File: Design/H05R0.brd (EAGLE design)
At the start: 60 x 34.6 mm, 59 parts, among them Q1 ECH8693R-TL-W, U1 STM32G0B1CEU6N, U2 MAX17330X22+, U3 TPS631000DRLR, U4 LD39200PU33R, X1 XTALL_CSTCE8M00G52

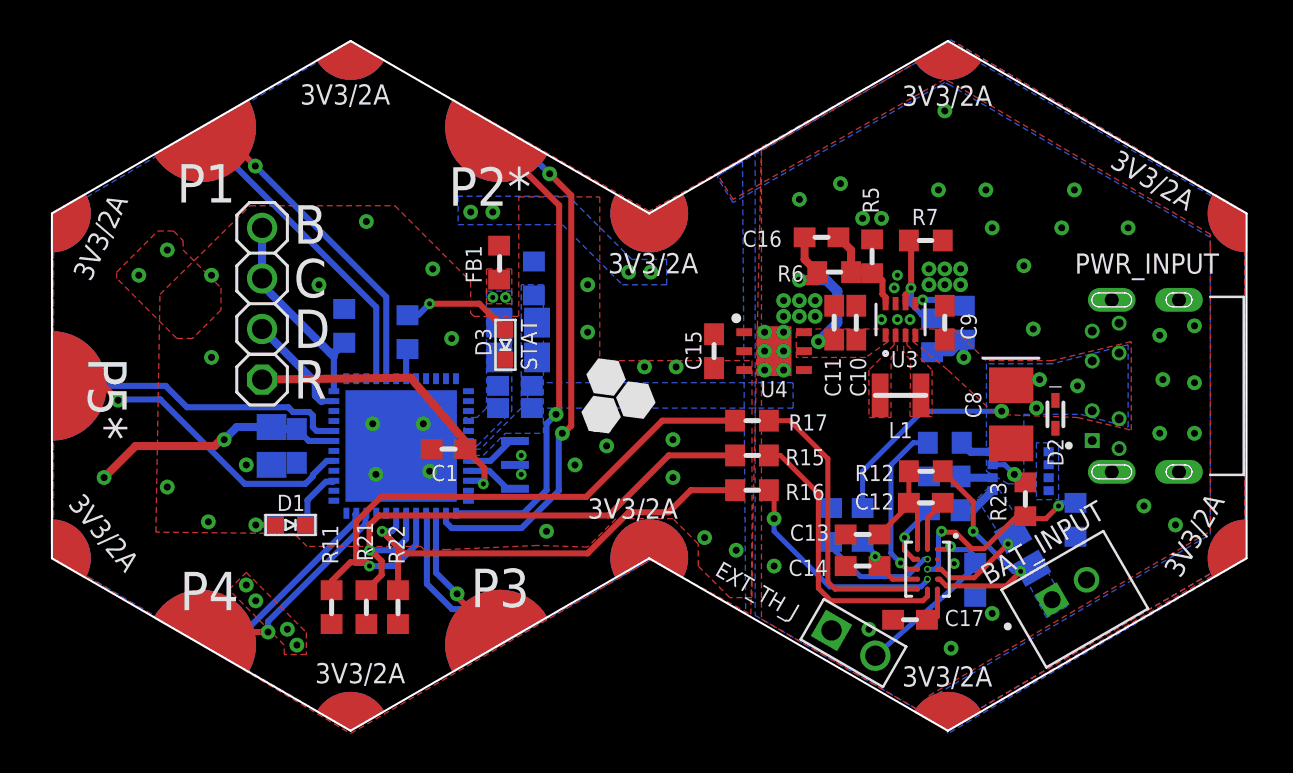
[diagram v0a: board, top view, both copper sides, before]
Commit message: -Adding wire to board terminal block
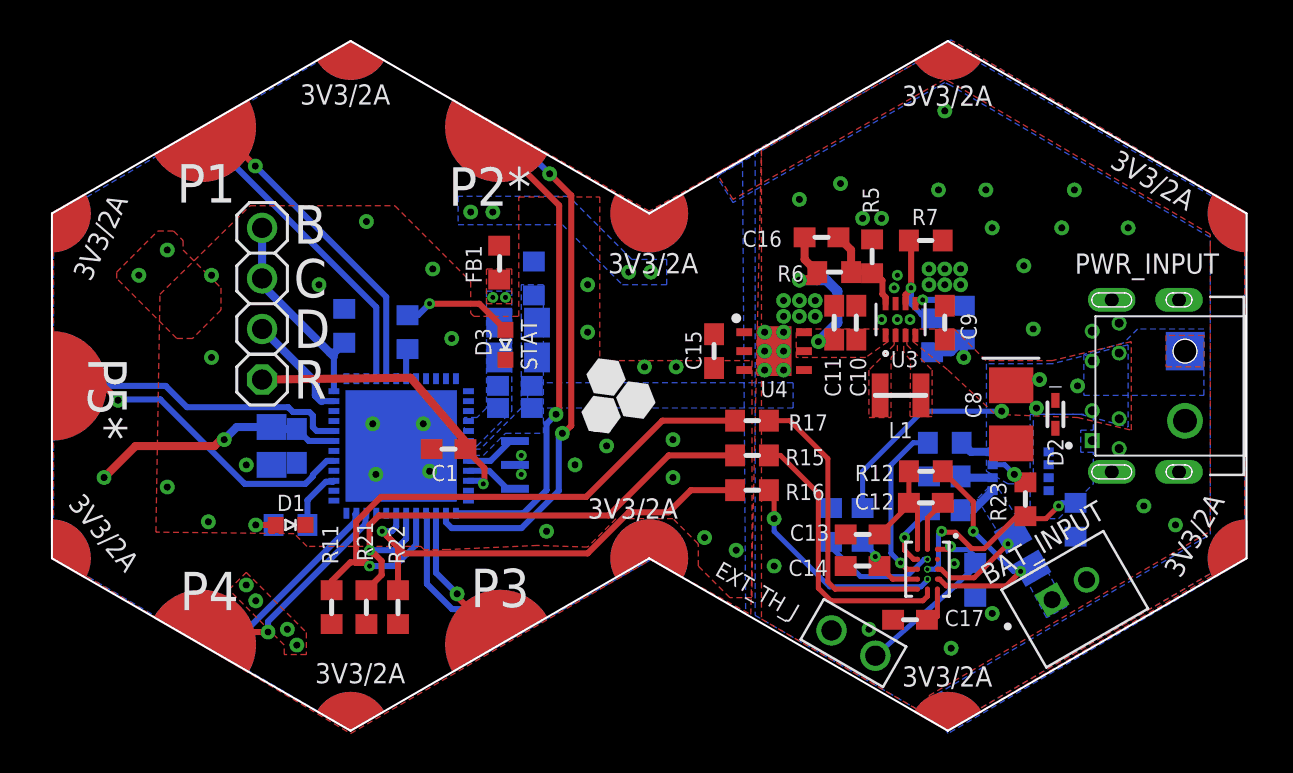
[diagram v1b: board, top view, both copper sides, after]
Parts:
- added J1: 1984617_MOD, HEXABITZ_CONNECTION_PARTS:1984617_MOD
- D1: device Hexabitz:VLMS1300-GS08 -> HEXABITZ_USER_INTERFACE_PARTS:VLMS1300-GS08
- D3: value GREEN -> Green; device Hexabitz:VLMS1300-GS08 -> HEXABITZ_USER_INTERFACE_PARTS:VLMTG1300-GS08
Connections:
- net VBUS: now also J1.1
- net VSSA: now also J1.2

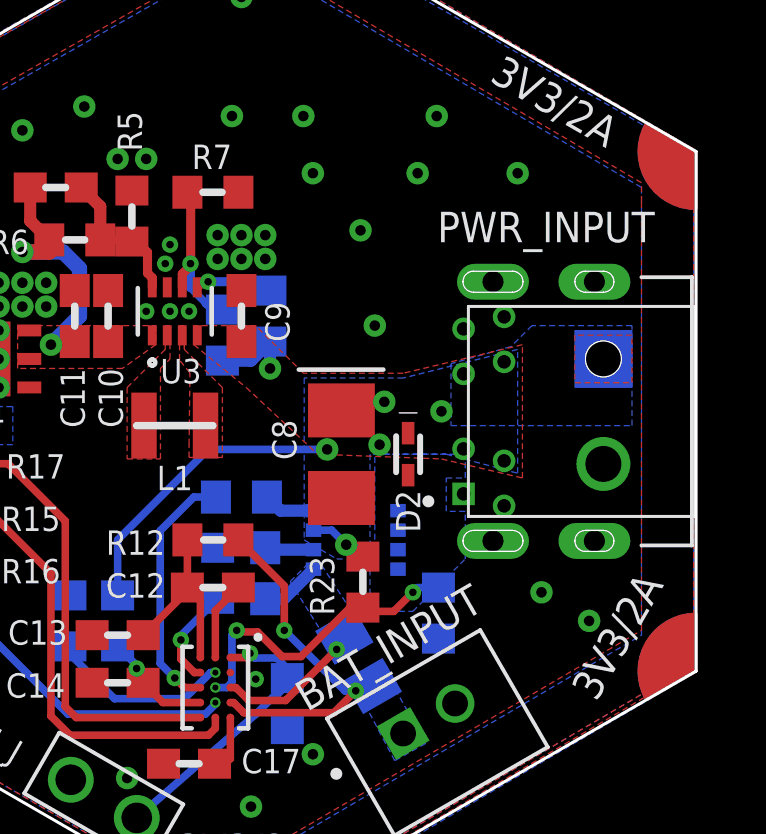
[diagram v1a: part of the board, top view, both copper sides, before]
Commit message: -Correcting the placement of the additional junction and including it in the Bill of Materials (BOM).
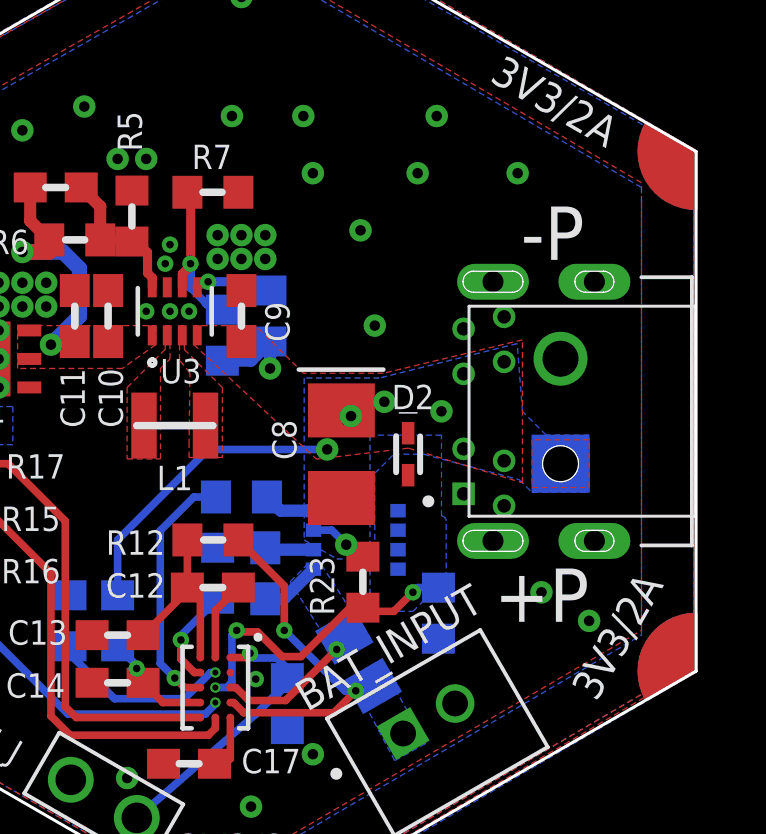
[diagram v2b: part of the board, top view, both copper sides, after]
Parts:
- moved J1 3.77 mm to (25.6, 6.99), turned to 90 degrees
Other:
- board text added: "+"
- board text added: "+P"
- board text added: "-"
- board text added: "-P"
- board text removed: "PWR_INPUT"

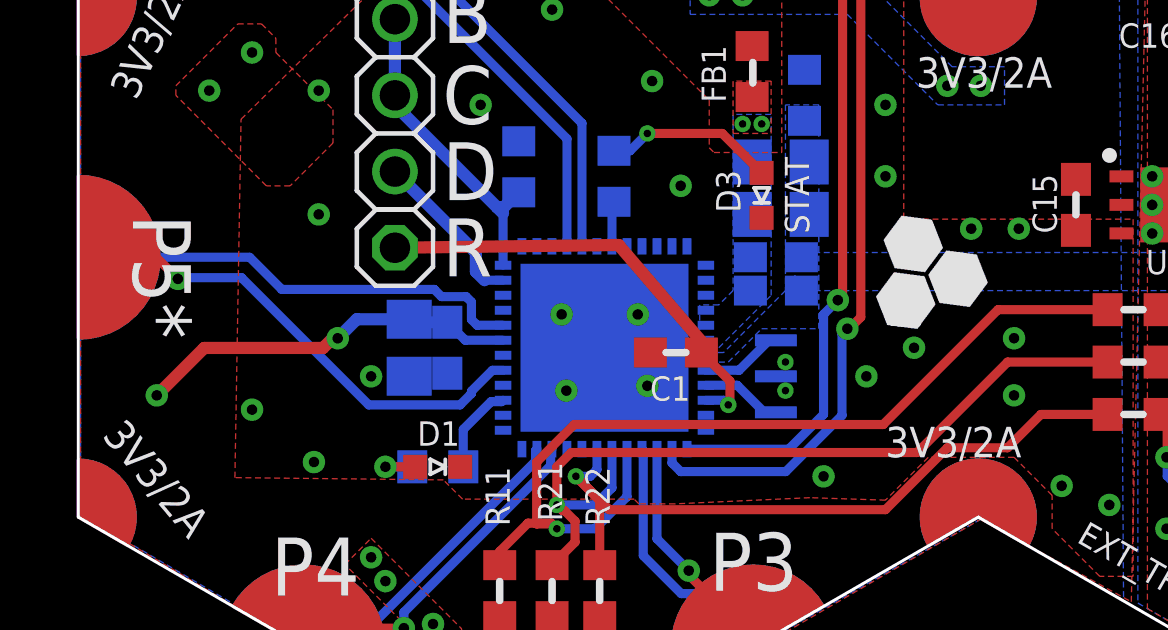
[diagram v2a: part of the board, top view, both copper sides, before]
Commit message: -Update the logo and add TVS
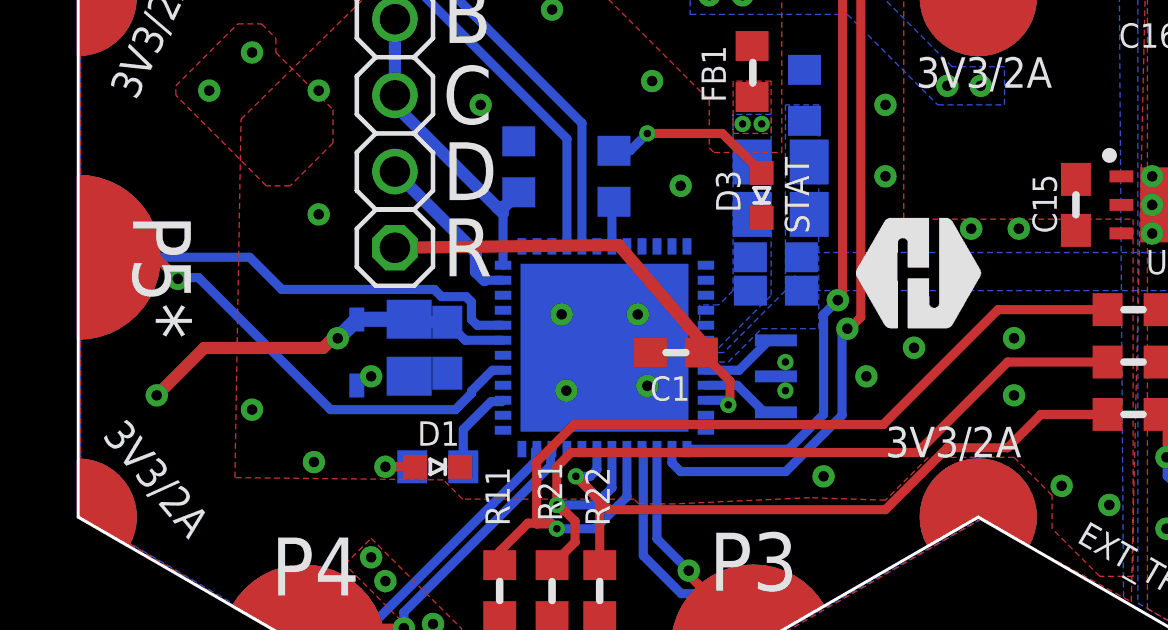
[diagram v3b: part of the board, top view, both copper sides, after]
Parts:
- added D4: BOURNS_CDSOD323-T03SCBOURNS_CDSOD323-T03SC_0_0, HEXABITZ_RCLS:BOURNS_CDSOD323-T03SC_0
- added TRIMBLE-LOGO1: HEXA-LOGO, HEXABITZ_USER_INTERFACE_PARTS:HEXA-LOGO
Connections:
- net GND: now also D4.1
- net VDD: now also D4.2
